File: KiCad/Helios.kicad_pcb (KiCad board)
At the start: 2 copper layers, 99.5 x 88 mm, 72 parts, among them CON1 AVR-JTAG-10, J1 Conn_01x04, J10 Conn_01x10, J11 Conn_01x16, J2 Conn_01x04, J3 Conn_01x04, J4 Conn_01x04, J5 Conn_01x04, J6 Conn_01x04, J7 Conn_01x11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

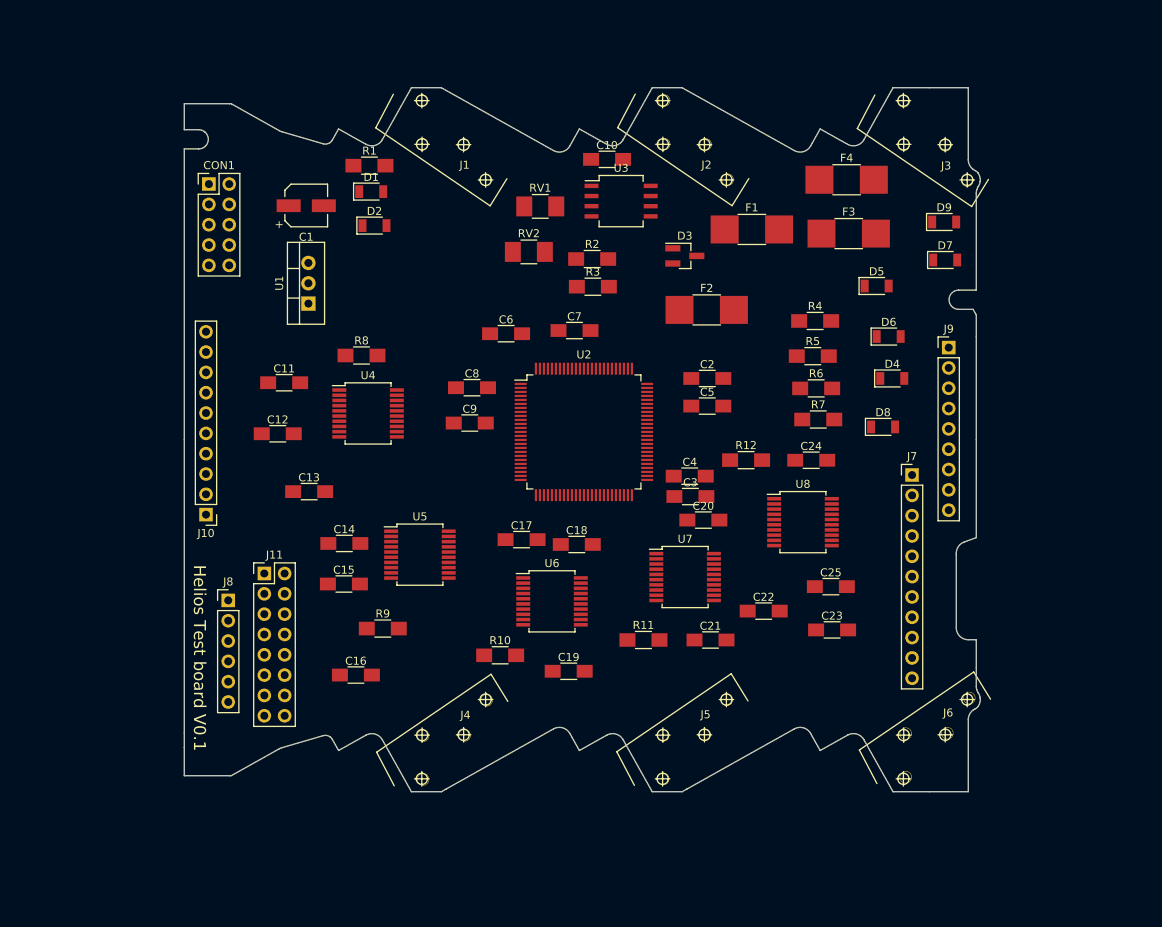
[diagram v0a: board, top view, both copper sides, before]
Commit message: start board routing
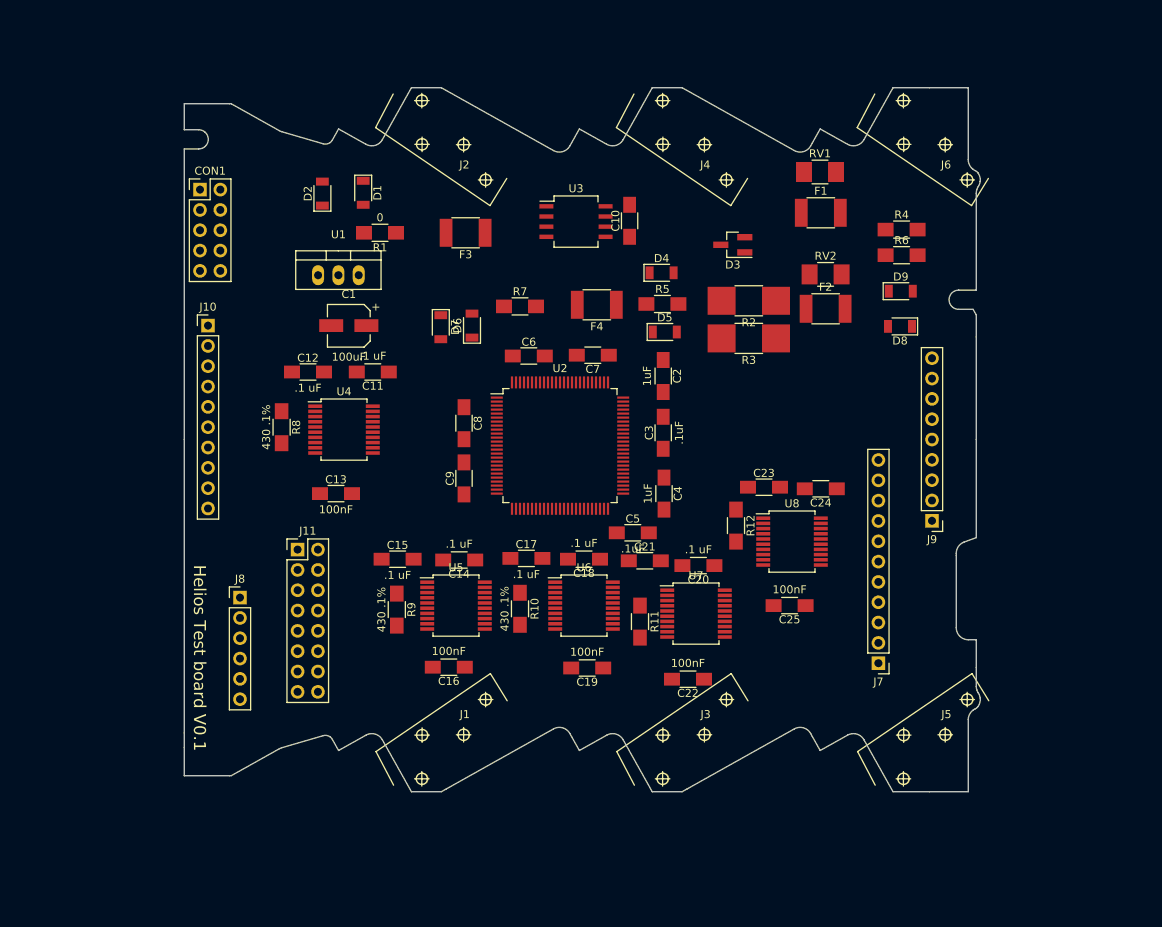
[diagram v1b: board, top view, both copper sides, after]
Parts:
- F1, F2, F3, F4: footprint Resistors_SMD:R_1812_HandSoldering -> Resistors_SMD:R_1812
- J1, J3: footprint CH20M:CH20Mt -> CH20M:CH20Mr
- J4, J6: footprint CH20M:CH20Mr -> CH20M:CH20Mt
- R2, R3: footprint Resistors_SMD:R_1206_HandSoldering -> Resistors_SMD:R_1812_HandSoldering
- U1: footprint TO_SOT_Packages_THT:TO-220-3_Vertical -> TO_SOT_Packages_THT:TO-220_Neutral123_Vertical
- moved J4 80.4 mm to (152.0, 51.9), turned to 0 degrees
- moved J3 80.3 mm to (152.4, 126.6), turned to 180 degrees
- moved J1 74.7 mm to (122.3, 126.6), turned to 180 degrees
- moved J6 74.5 mm to (182.1, 51.9), turned to 0 degrees
- moved D7 63.6 mm to (121.1, 75.2), turned to 270 degrees
- moved D6 52.1 mm to (125.0, 75.0), turned to 90 degrees
- moved F3 47.9 mm to (124.2, 63.4), turned to 180 degrees
- moved R7 39.9 mm to (131.0, 72.6)
- moved RV2 37.2 mm to (169.2, 68.6)
- moved RV1 35.2 mm to (168.5, 55.8)
- moved F4 34.9 mm to (140.6, 72.4), turned to 180 degrees
- moved D4 31.7 mm to (148.7, 68.4)
- moved J2 30.3 mm to (121.9, 51.9)
- moved J5 30.1 mm to (182.5, 126.6)
- moved D5 27.1 mm to (149.1, 75.8)
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
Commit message: make changes to rx/tx lights
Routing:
- net +3V3: track 0.00 -> 389.5 mm, vias 0 -> 4
- net Net-(J7-Pad3): track 0.00 -> 148.6 mm, vias 0 -> 2
- net /GPIOB/~CS: track 0.00 -> 126.9 mm, vias 0 -> 1
- net /GPIOA/485RX: track 0.00 -> 123.5 mm
- net RTD_SCK: track 0.00 -> 120.2 mm, vias 0 -> 3
- net RTD_MISO: track 0.00 -> 120.1 mm, vias 0 -> 4
- net RTD_MOSI: track 0.00 -> 114.4 mm, vias 0 -> 2
- net RTD-1: track 0.00 -> 103.3 mm, vias 0 -> 1
- net /GPIOA/485TX: track 0.00 -> 100.3 mm, vias 0 -> 1
- net Net-(J9-Pad7): track 0.00 -> 100.0 mm, vias 0 -> 2
- net /GPIOB/~RST: track 0.00 -> 95.5 mm, vias 0 -> 1
- net GND: track 0.00 -> 77.9 mm, vias 0 -> 43
- net RTDb1: track 0.00 -> 76.1 mm, vias 0 -> 1
- net /GPIOB/UART1_TX: track 0.00 -> 74.8 mm, vias 0 -> 1
- net /GPIOB/MOSI: track 0.00 -> 74.0 mm, vias 0 -> 2
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- added copper zone on B.Cu, net GND

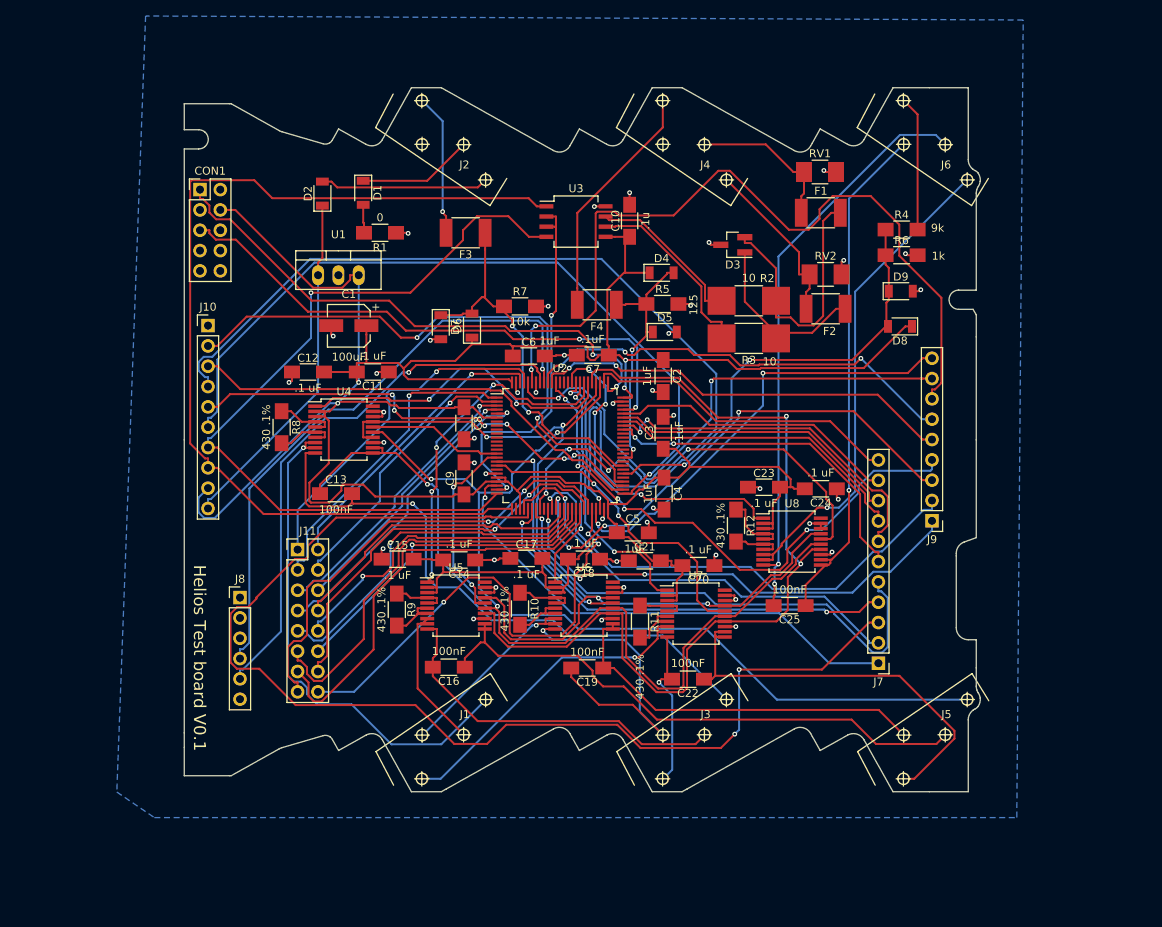
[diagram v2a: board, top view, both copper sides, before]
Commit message: change outline to new pattern
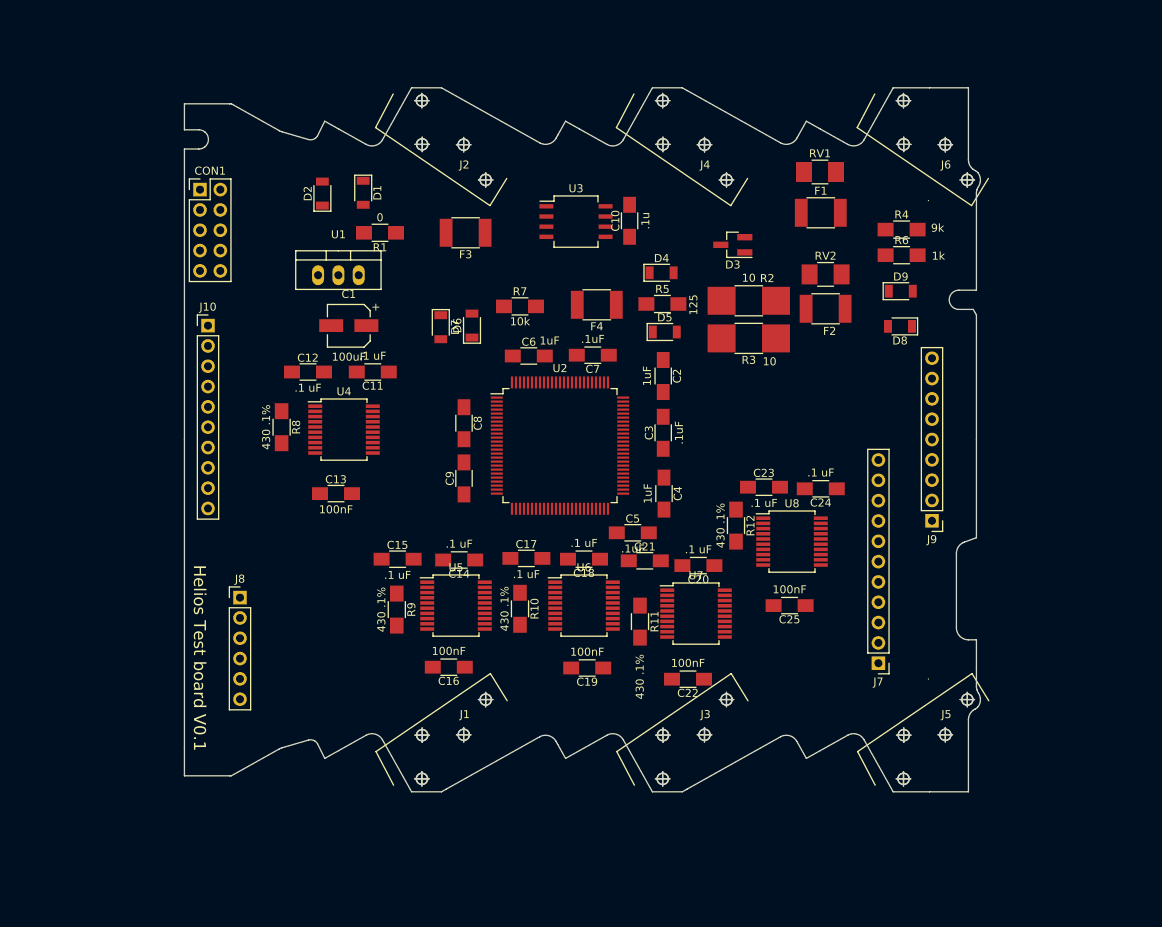
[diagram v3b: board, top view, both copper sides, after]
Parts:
- removed J11: Conn_01x16, Pin_Headers:Pin_Header_Straight_2x08_Pitch2.54mm
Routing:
- net +3V3: track 389.5 -> 0.00 mm, vias 4 -> 0
- net Net-(J7-Pad3): track 148.6 -> 0.00 mm, vias 2 -> 0
- net /GPIOB/~CS: track 126.9 -> 0.00 mm, vias 1 -> 0
- net /GPIOA/485RX: track 123.5 -> 0.00 mm
- net RTD_SCK: track 120.2 -> 0.00 mm, vias 3 -> 0
- net RTD_MISO: track 120.1 -> 0.00 mm, vias 4 -> 0
- net RTD_MOSI: track 114.4 -> 0.00 mm, vias 2 -> 0
- net RTD-1: track 103.3 -> 0.00 mm, vias 1 -> 0
- net /GPIOA/485TX: track 100.3 -> 0.00 mm, vias 1 -> 0
- net Net-(J9-Pad7): track 100.0 -> 0.00 mm, vias 2 -> 0
- net /GPIOB/~RST: track 95.5 -> 0.00 mm, vias 1 -> 0
- net GND: track 77.9 -> 0.00 mm, vias 43 -> 0
- net RTDb1: track 76.1 -> 0.00 mm, vias 1 -> 0
- net /GPIOB/UART1_TX: track 74.8 -> 0.00 mm, vias 1 -> 0
- net /GPIOB/MOSI: track 74.0 -> 0.00 mm, vias 2 -> 0
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- removed copper zone on B.Cu, net GND
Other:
- outline, holes or cut-outs redrawn

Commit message: getting ready to submit board
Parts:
- added J11: GS3, Connectors:GS3, F.Cu at (165.1, 58.7)
- added J12: GS3, Connectors:GS3, F.Cu at (170.7, 58.7)
- added J13: GS3, Connectors:GS3, F.Cu at (176.0, 58.7)
- moved J8 90.3 mm to (182.8, 84.0)
- moved J9 83.4 mm to (99.1, 98.3), turned to 90 degrees
- moved J7 82.3 mm to (98.0, 90.6)
- moved CON1 79.1 mm to (160.3, 96.1), turned to 90 degrees
- moved R4 29.0 mm to (158.5, 83.8), turned to 180 degrees
- moved C11 23.6 mm to (106.8, 103.6)
- moved C12 23.4 mm to (98.7, 103.5)
- moved R8 23.1 mm to (96.5, 110.4)
- moved U4 22.9 mm to (103.9, 110.4)
- moved D8 22.2 mm to (159.5, 86.6), turned to 0 degrees
- moved R6 22.0 mm to (165.6, 83.9)
- moved C13 21.8 mm to (103.8, 117.3)
- moved D9 21.2 mm to (164.6, 86.6)
- moved R12 16.6 mm to (169.7, 111.7)
- moved R5 16.5 mm to (144.3, 56.4)
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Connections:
- C10 pad 1: +3V3 -> GND
- C10 pad 2: GND -> +3V3
- J10 pad 7: /GPIOA/485TX -> /GPIOB/485TX
- J10 pad 8: /GPIOA/485RX -> /GPIOB/485RX
- J6 pad 1: RTDa5 -> Net-(J11-Pad2)
- J6 pad 2: RTDb5 -> Net-(J12-Pad2)
- J6 pad 3: RTD-5 -> Net-(J13-Pad2)
- J8 pad 4: /GPIOB/UART1_TX -> /GPIOB/UART1_RX
- J8 pad 5: /GPIOB/UART1_RX -> /GPIOB/UART1_TX
- U2 pad 25: /GPIOA/485TX -> /GPIOA/serial/TX
- U2 pad 26: /GPIOA/485RX -> /GPIOA/serial/RX
- U2 pad 59: Net-(U2-Pad59) -> Net-(D6-Pad2)
- U2 pad 63: Net-(U2-Pad63) -> Rain
- U2 pad 64: Net-(U2-Pad64) -> Aux
- U2 pad 97: Net-(J11-Pad1) -> /GPIOB/485RX
- U2 pad 98: Net-(J11-Pad2) -> /GPIOB/485TX
- U3 pad 1: /GPIOA/485RX -> /GPIOA/serial/RX
- U3 pad 4: /GPIOA/485TX -> /GPIOA/serial/TX
- U3 pad 5: +3V3 -> GND
- U3 pad 8: GND -> +3V3
- U4 pad 14: RTD_MISO -> RTD_MOSI
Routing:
- net GND: track 0.00 -> 566.5 mm, vias 0 -> 1
- net +3V3: track 0.00 -> 367.6 mm, vias 0 -> 6
- net RTD_MISO: track 0.00 -> 128.3 mm, vias 0 -> 3
- net RTD_SCK: track 0.00 -> 125.7 mm, vias 0 -> 3
- net RTD_MOSI: track 0.00 -> 119.9 mm, vias 0 -> 5
- net RTD-1: track 0.00 -> 94.0 mm, vias 0 -> 2
- net /GPIOB/~RST: track 0.00 -> 76.7 mm, vias 0 -> 1
- net RTD-2: track 0.00 -> 73.7 mm
- net RTDb5: track 0.00 -> 71.6 mm
- net RTD-5: track 0.00 -> 70.0 mm
- net /GPIOB/D/~C: track 0.00 -> 69.5 mm, vias 0 -> 1
- net RTDa5: track 0.00 -> 69.0 mm
- net /GPIOB/SCK: track 0.00 -> 68.1 mm, vias 0 -> 1
- net /GPIOB/MOSI: track 0.00 -> 66.1 mm, vias 0 -> 1
- net RTDb1: track 0.00 -> 65.7 mm, vias 0 -> 1
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- added copper zone on B.Cu, net GND
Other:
- outline, holes or cut-outs redrawn
- board text added: "Helios Test board V0.5"
- board text removed: "Helios Test board V0.1"

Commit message: compiled board zip file for export
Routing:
- added copper zone on F.Cu, net GND
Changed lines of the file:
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@@
     (polygon
       (pts
-        (xy 85.575 43.425) (xy 196.725 43.425) (xy 196.1 142.375) (xy 79.275 141.775) (xy 82.725 46.675)
+        (xy 196.401565 94.631232) (xy 206.25 95.75) (xy 203.575 147.075) (xy 72.4 144.025) (xy 70.875 85.1)
+        (xy 71.125 80.4) (xy 81.458951 81.573922) (xy 82.725 46.675) (xy 85.575 43.425) (xy 196.725 43.425)
       )
     )
+  )
+  (zone (net 2) (net_name GND) (layer F.Cu) (hatch edge 0.508)
+    (connect_pads (clearance 0.508))
+    (min_thickness 0.254)
+    (fill yes (arc_segments 16) (thermal_gap 0.508) (thermal_bridge_width 0.508))
+    (polygon
+      (pts
+        (xy 69.2 40.85) (xy 68 148.125) (xy 209.2 147.725) (xy 209 40.025)
+      )
+    )

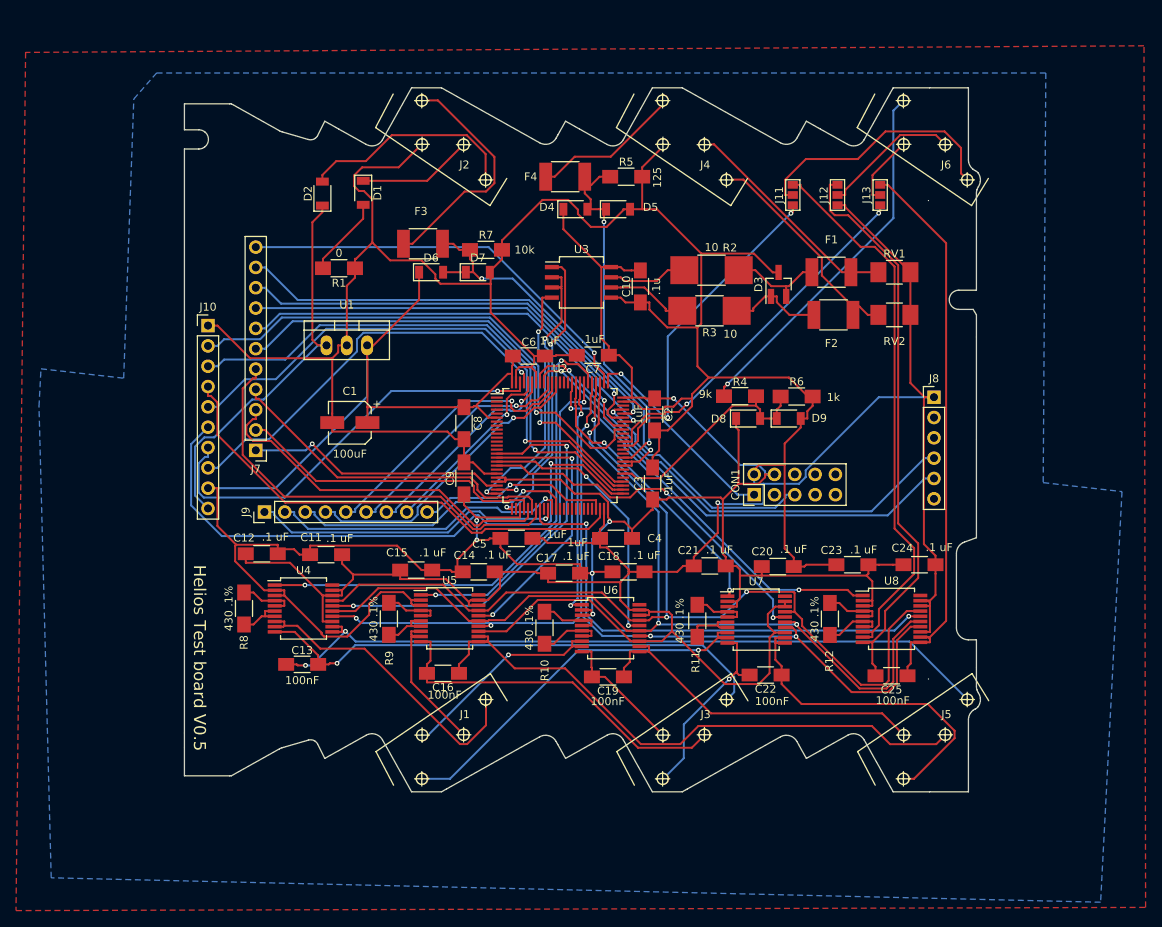
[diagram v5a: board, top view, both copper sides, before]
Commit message: changed board outline
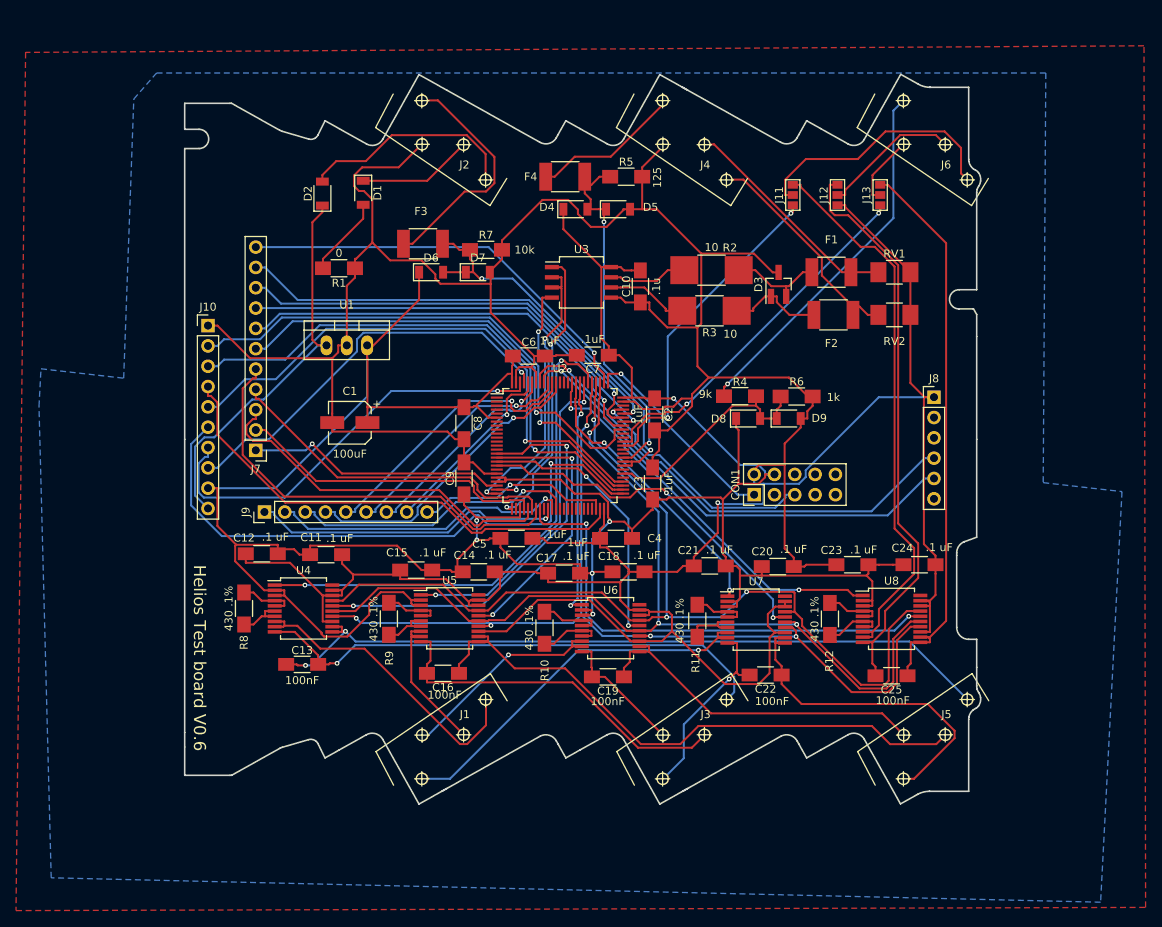
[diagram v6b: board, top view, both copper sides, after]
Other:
- board size 99.5 x 88 mm -> 99.5 x 91.2 mm
- board text added: "Helios Test board V0.6"
- board text removed: "Helios Test board V0.5"
